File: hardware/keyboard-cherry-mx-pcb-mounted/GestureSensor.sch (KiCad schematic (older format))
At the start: 2 parts

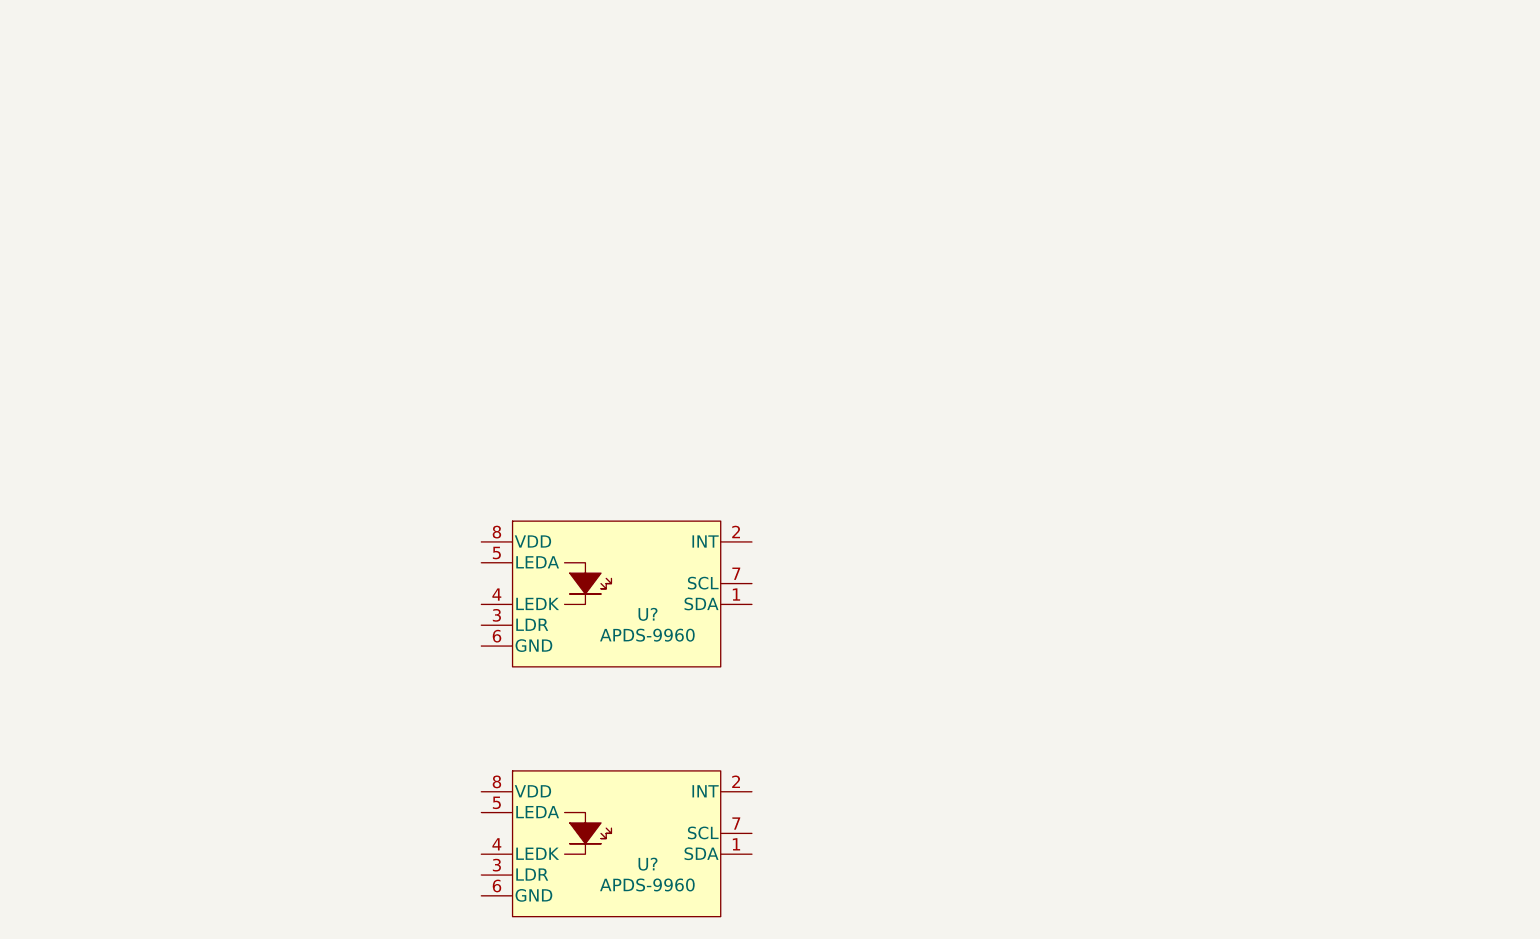
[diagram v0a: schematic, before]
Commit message: Adds gesture sensor interface. May change to bigger stm32 package.
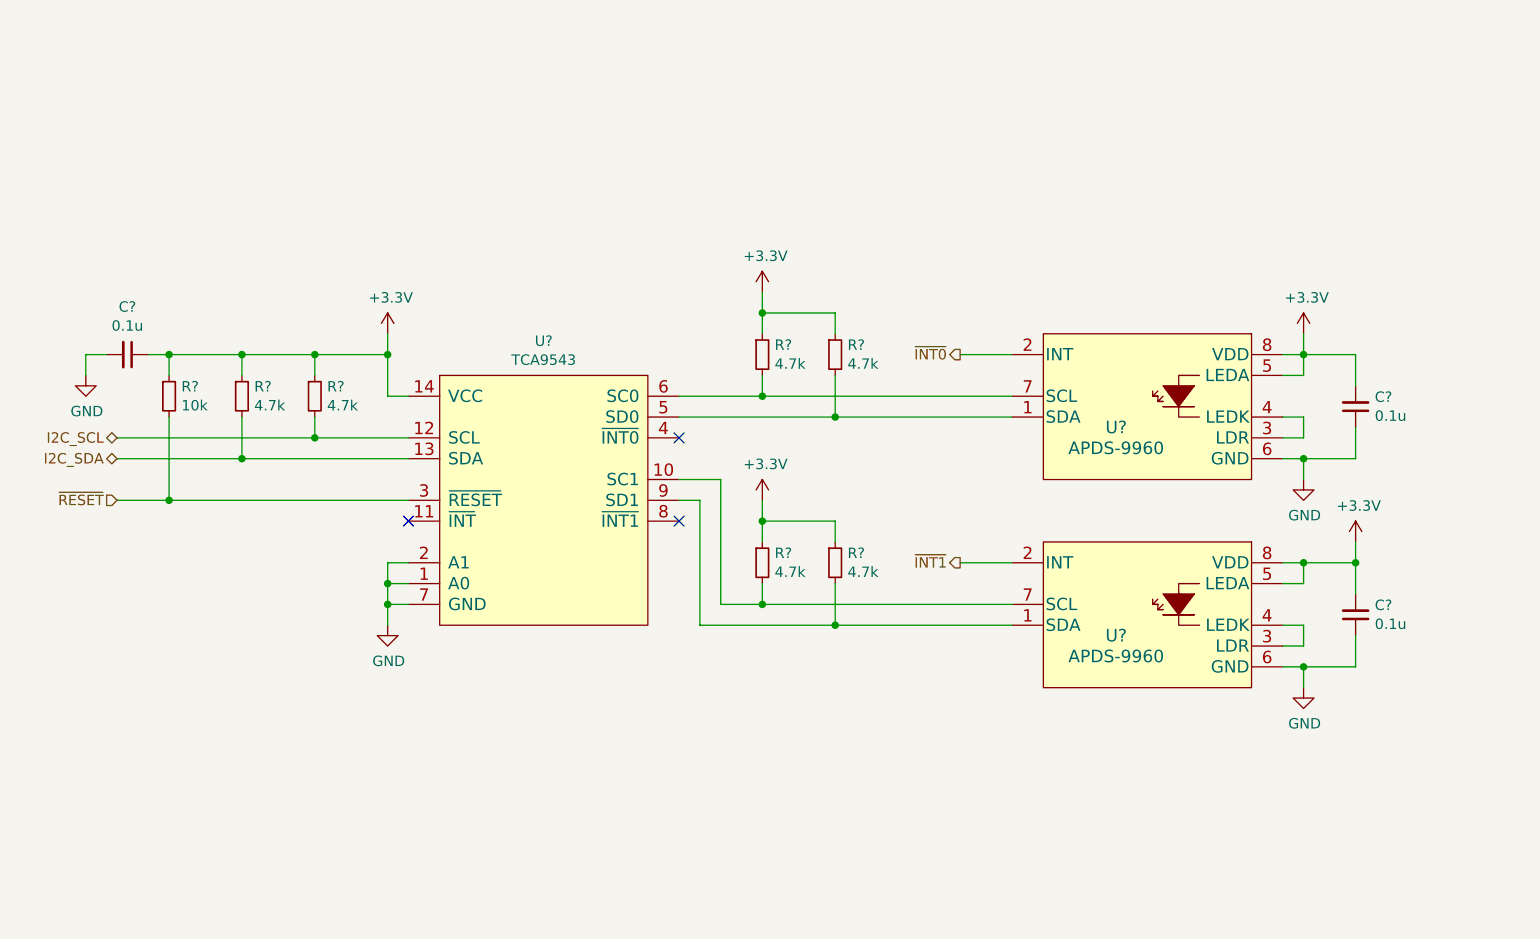
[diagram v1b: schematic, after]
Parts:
- added C? (x3): 0.1u, symbol Device:C_Small
- added R?: 10k, Resistor_SMD:R_0805_2012Metric, symbol Device:R_Small
- added R? (x6): 4.7k, Resistor_SMD:R_0805_2012Metric, symbol Device:R_Small
- added U?: TCA9543, Package_SO:SOIC-14_3.9x8.7mm_P1.27mm, symbol Sij_MUX:TCA9543
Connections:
- net at U?.1 (SDA): now also R?.2, U?.5 (SD0)
- net ~INT0: now reaches U?.2 (INT)
- net at U?.3 (LDR): now also U?.4 (LEDK) (x2)
- net +3V3: now reaches U?.5 (LEDA)
- net +3V3: now also U?.5 (LEDA), U?.8 (VDD), U?.8 (VDD), C?.1, C?.2, C?.2, R?.1, R?.1, R?.1, R?.1, R?.1, R?.1, R?.1, U?.14 (VCC)
- net GND: now reaches U?.6 (GND)
- net GND: now also U?.6 (GND), C?.1, C?.1, C?.2, U?.1 (A0), U?.2 (A1), U?.7 (GND)
- net at U?.7 (SCL): now also R?.2, U?.6 (SC0)
- net at U?.1 (SDA): now also R?.2, U?.9 (SD1)
- net ~INT1: now reaches U?.2 (INT)
- net at U?.7 (SCL): now also R?.2, U?.10 (SC1)
- new net I2C_SCL: R?.2, U?.12 (SCL)
- new net I2C_SDA: R?.2, U?.13 (SDA)
- new net ~RESET: R?.2, U?.3 (~RESET)
- no-connect marks 0 -> 3
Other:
- moved on the sheet: U?

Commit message: Adds completed sensor and power connections. Still need to add USB footprint then sch are done for version 1.0
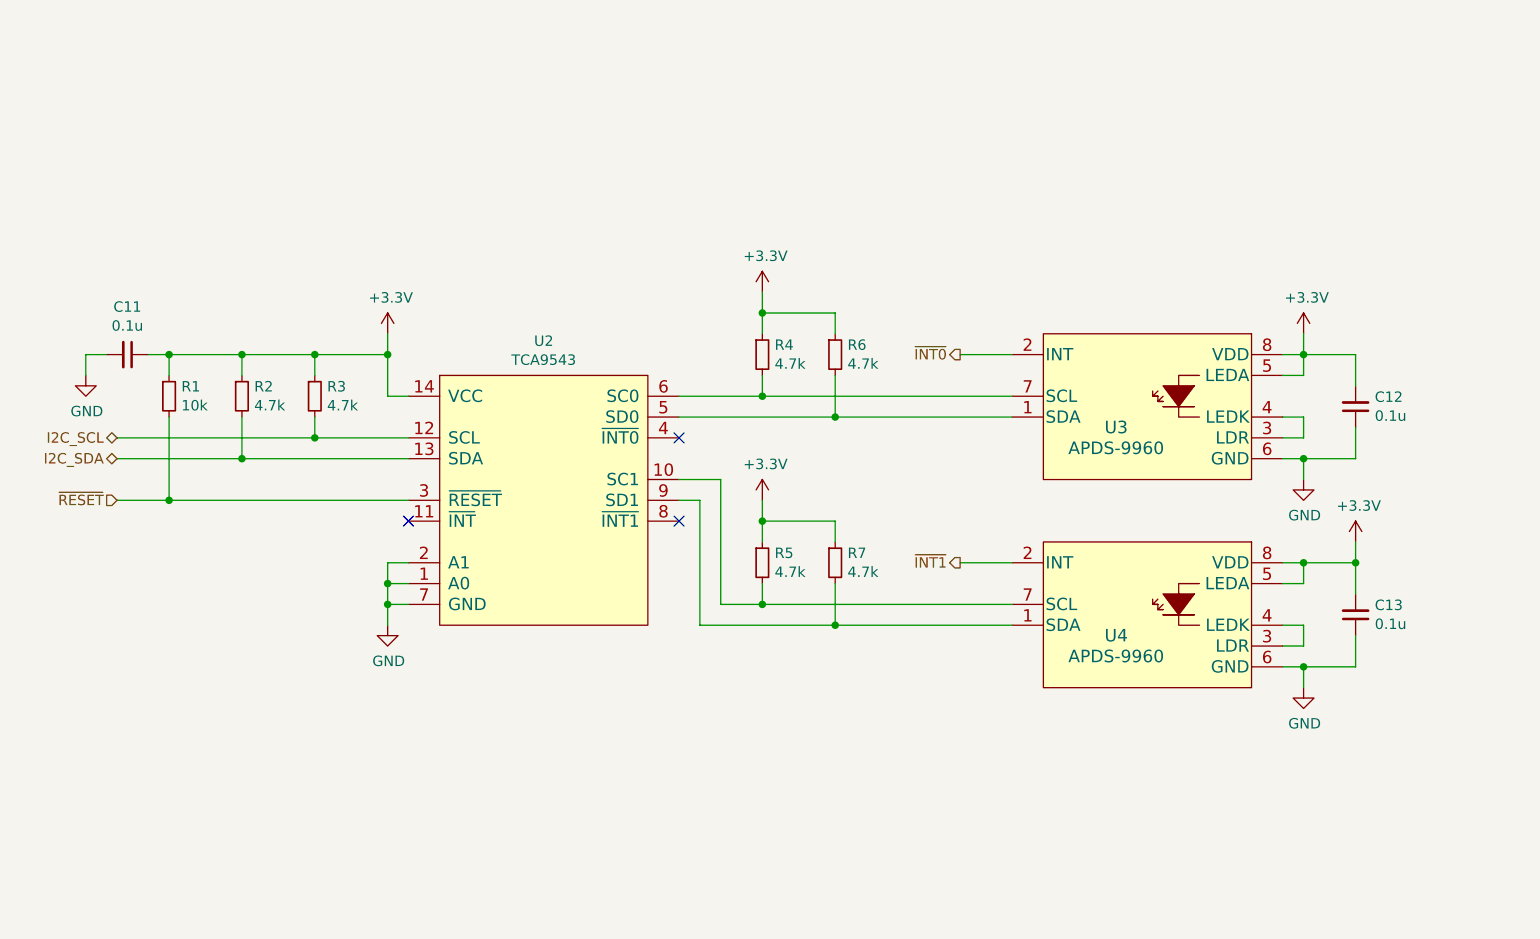
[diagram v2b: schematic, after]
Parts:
- C11, C12, C13: renamed from C?; footprint (none) -> Capacitor_SMD:C_0805_2012Metric
- U3, U4: renamed from U?; footprint QFN_DS-9930 -> Sij_Sensors:APDS-9930
- gave numbers to parts that had none: 8

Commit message: Adds more gesture sensors to the cherry mx pcb mounted keyboard.
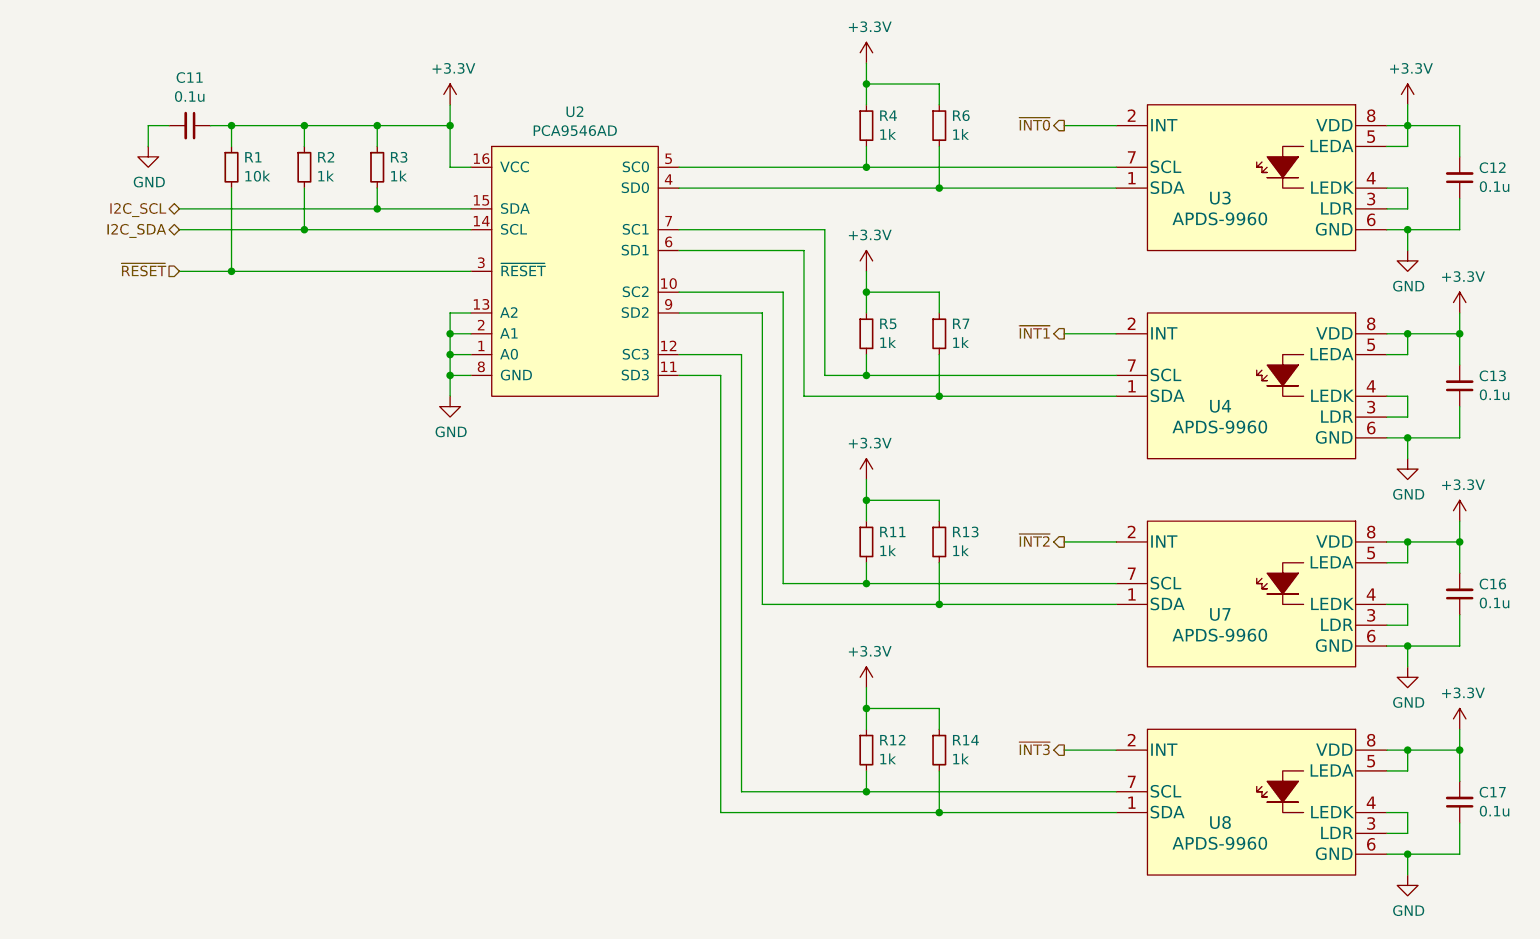
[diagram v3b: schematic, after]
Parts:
- removed U2: TCA9543, Package_SO:SOIC-14_3.9x8.7mm_P1.27mm, symbol Sij_MUX:TCA9543
- added C16, C17: 0.1u, Capacitor_SMD:C_0805_2012Metric, symbol Device:C_Small
- added R11, R12, R13, R14: 1k, Resistor_SMD:R_0805_2012Metric, symbol Device:R_Small
- added U2: PCA9546AD, Package_SO:SOIC-16_3.9x9.9mm_P1.27mm, symbol Sij_MUX:PCA9546AD
- added U7, U8: APDS-9960, Sij_Sensors:APDS-9930, symbol Sij_Sensors:APDS-9930
- R2, R3, R4, R5, R6, R7: value 4.7k -> 1k
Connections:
- net +3V3: now also C16.2, C17.2, R11.1, R12.1, R13.1, R14.1, U2.16 (VCC), U7.5 (LEDA), U7.8 (VDD), U8.5 (LEDA), U8.8 (VDD)
- net GND: now also C16.1, C17.1, U2.1 (A0), U2.13 (A2), U2.2 (A1), U2.8 (GND), U7.6 (GND), U8.6 (GND)
- net I2C_SCL: now also U2.15 (SDA)
- net I2C_SDA: now also U2.14 (SCL)
- net ~RESET: now also U2.3 (~RESET)
- net at R6.2, U3.1 (SDA): now also U2.4 (SD0)
- net at R4.2, U3.7 (SCL): now also U2.5 (SC0)
- net at R7.2, U4.1 (SDA): now also U2.6 (SD1)
- net at R5.2, U4.7 (SCL): now also U2.7 (SC1)
- new net: R11.2, U2.10 (SC2), U7.7 (SCL)
- new net: R14.2, U2.11 (SD3), U8.1 (SDA)
- new net: R12.2, U2.12 (SC3), U8.7 (SCL)
- new net: R13.2, U2.9 (SD2), U7.1 (SDA)
- new net: U7.3 (LDR), U7.4 (LEDK)
- new net: U8.3 (LDR), U8.4 (LEDK)
- new net ~INT2: U7.2 (INT)
- new net ~INT3: U8.2 (INT)
- no-connect marks 3 -> 0
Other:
- moved on the sheet: C11, C12, C13, R1, R2, R3, R4, R5, R6, R7, U3, U4
